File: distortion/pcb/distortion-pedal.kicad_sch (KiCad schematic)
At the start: 24 parts, among them U2 TL081H, U4 TL081H

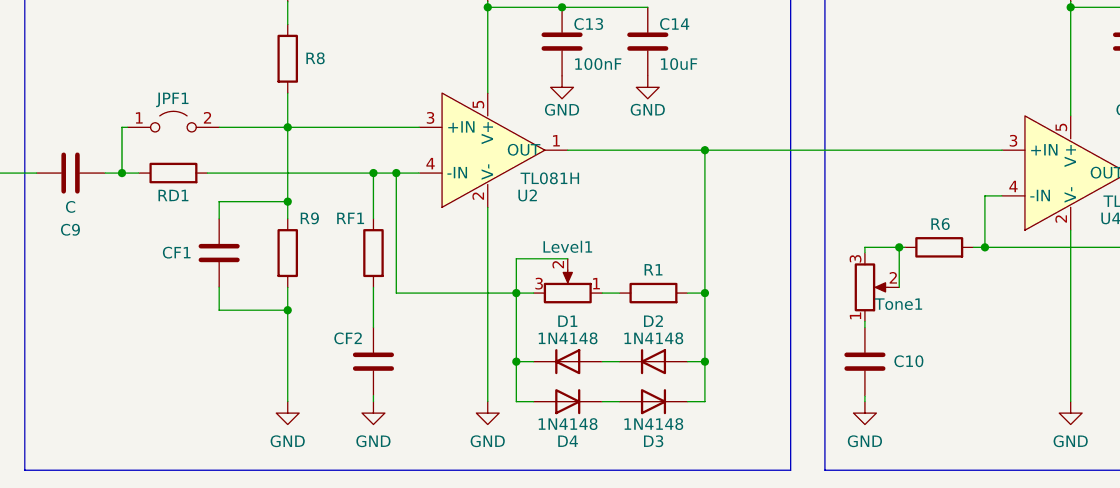
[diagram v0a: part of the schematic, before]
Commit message: add circuit dimensioning
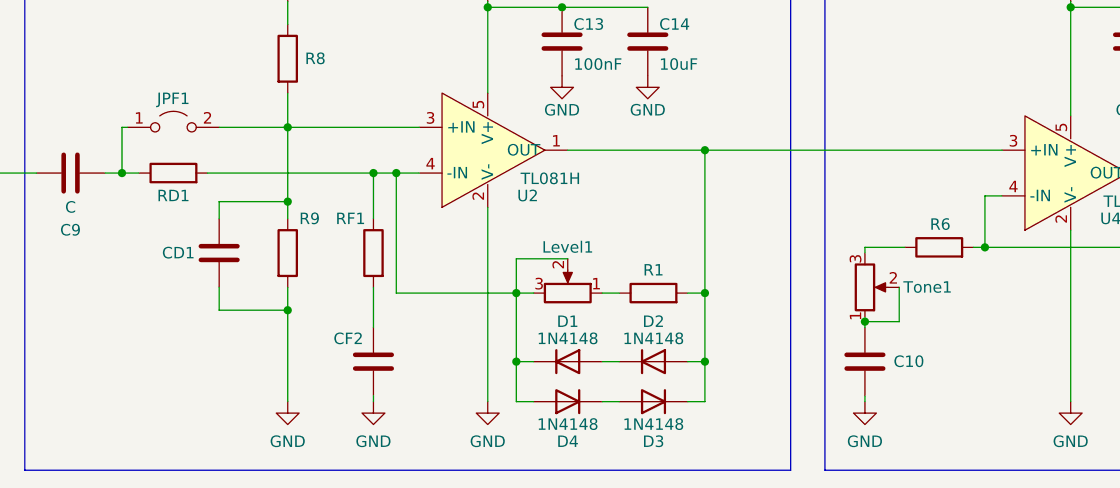
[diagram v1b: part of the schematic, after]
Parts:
- renumbered CF1 to CD1
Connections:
- net at C10.1, Tone1.1: now also Tone1.2
- net at R6.1, Tone1.3: no longer Tone1.2
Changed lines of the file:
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@@
   (junction (at 108.585 85.09) (diameter 0) (color 0 0 0 0)
   )
+  (junction (at 126.365 80.645) (diameter 0) (color 0 0 0 0)
+  )
   (junction (at 62.23 59.055) (diameter 0) (color 0 0 0 0)
   )
@@
   (junction (at 87.63 85.09) (diameter 0) (color 0 0 0 0)
   )
-  (junction (at 130.175 72.39) (diameter 0) (color 0 0 0 0)
-  )
   (wire (pts (xy 62.23 67.31) (xy 62.23 69.215))
     (stroke (width 0) (type default) (color 0 0 0 0))
@@
     (stroke (width 0) (type default) (color 0 0 0 0))
   )
-  (wire (pts (xy 130.81 72.39) (xy 130.175 72.39))
-    (stroke (width 0) (type default) (color 0 0 0 0))
-  )
   (wire (pts (xy 43.815 59.055) (xy 44.45 59.055))
     (stroke (width 0) (type default) (color 0 0 0 0))
@@
     (stroke (width 0) (type default) (color 0 0 0 0))
   )
+  (wire (pts (xy 130.175 80.645) (xy 126.365 80.645))
+    (stroke (width 0) (type default) (color 0 0 0 0))
+  )
   (wire (pts (xy 71.755 76.835) (xy 71.755 81.28))
     (stroke (width 0) (type default) (color 0 0 0 0))
@@
     (stroke (width 0) (type default) (color 0 0 0 0))
   )
-  (wire (pts (xy 130.175 72.39) (xy 130.175 76.835))
-    (stroke (width 0) (type default) (color 0 0 0 0))
-  )
   (wire (pts (xy 53.34 64.135) (xy 71.755 64.135))
     (stroke (width 0) (type default) (color 0 0 0 0))
@@
     (stroke (width 0) (type default) (color 0 0 0 0))
   )
+  (wire (pts (xy 130.175 76.835) (xy 130.175 80.645))
+    (stroke (width 0) (type default) (color 0 0 0 0))
+  )
   (wire (pts (xy 62.23 59.055) (xy 76.835 59.055))
     (stroke (width 0) (type default) (color 0 0 0 0))
@@
     (stroke (width 0) (type default) (color 0 0 0 0))
   )
-  (wire (pts (xy 130.175 72.39) (xy 126.365 72.39))
+  (wire (pts (xy 126.365 72.39) (xy 130.81 72.39))
     (stroke (width 0) (type default) (color 0 0 0 0))
   )
@@
   (symbol (lib_id "Device:R_Potentiometer") (at 126.365 76.835 0) (mirror x) (unit 1)
     (in_bom yes) (on_board yes)
-    (property "Reference" "Tone1" (id 0) (at 130.175 78.74 0))
+    (property "Reference" "Tone1" (id 0) (at 133.35 76.835 0))
     (property "Value" "R" (id 1) (at 131.445 76.835 90)
       (effects (font (size 1.27 1.27)) hide)
@@
   (symbol (lib_id "Device:C") (at 54.61 73.025 0) (unit 1)
     (in_bom yes) (on_board yes)
-    (property "Reference" "CF1" (id 0) (at 48.26 73.025 0)
+    (property "Reference" "CD1" (id 0) (at 48.26 73.025 0)
       (effects (font (size 1.27 1.27)) (justify left))
     )
@@
     )
     (path "/cff3208d-ece8-4d14-a5bb-ad4303e25136"
-      (reference "CF1") (unit 1) (value "C") (footprint "Capacitor_SMD:C_0805_2012Metric_Pad1.18x1.45mm_HandSolder")
+      (reference "CD1") (unit 1) (value "C") (footprint "Capacitor_SMD:C_0805_2012Metric_Pad1.18x1.45mm_HandSolder")
     )
     (path "/8086bab7-7dd2-4a38-97a8-11275acbbd45"

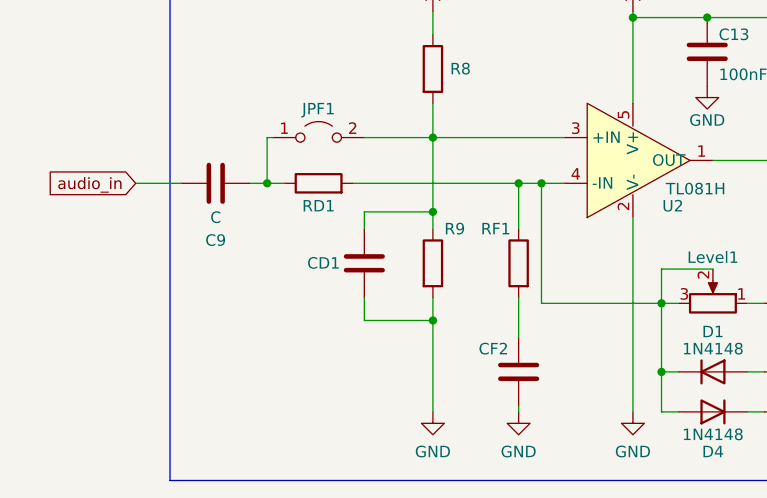
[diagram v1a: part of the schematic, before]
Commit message: add BOM, rework dimensioning
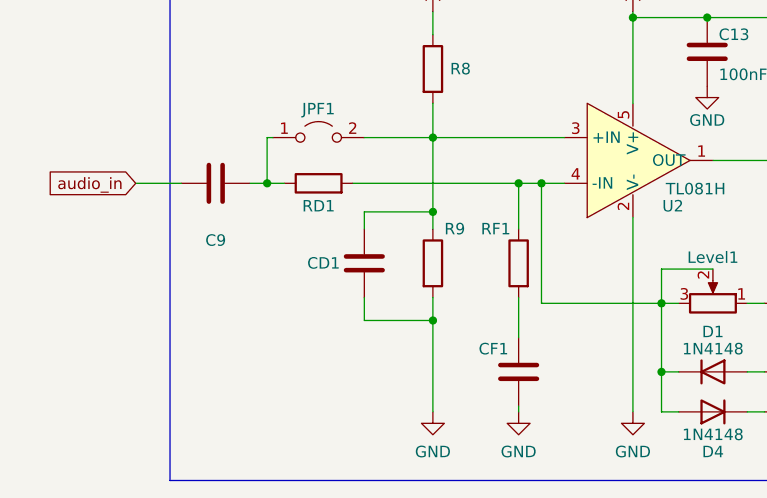
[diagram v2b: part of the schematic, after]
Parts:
- renumbered CF2 to CF1
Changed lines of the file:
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@@
     (in_bom yes) (on_board yes)
     (property "Reference" "C9" (id 0) (at 38.1 70.485 90))
-    (property "Value" "C" (id 1) (at 38.1 67.945 90))
+    (property "Value" "C" (id 1) (at 38.1 67.945 90)
+      (effects (font (size 1.27 1.27)) hide)
+    )
     (property "Footprint" "Capacitor_SMD:C_0805_2012Metric_Pad1.18x1.45mm_HandSolder" (id 2) (at 41.91 63.1698 0)
       (effects (font (size 1.27 1.27)) hide)
@@
   (symbol (lib_id "Device:C") (at 71.755 85.09 0) (unit 1)
     (in_bom yes) (on_board yes)
-    (property "Reference" "CF2" (id 0) (at 67.31 82.55 0)
+    (property "Reference" "CF1" (id 0) (at 67.31 82.55 0)
       (effects (font (size 1.27 1.27)) (justify left))
     )
@@
     )
     (path "/8086bab7-7dd2-4a38-97a8-11275acbbd45"
-      (reference "CF2") (unit 1) (value "C") (footprint "Capacitor_SMD:C_0805_2012Metric_Pad1.18x1.45mm_HandSolder")
+      (reference "CF1") (unit 1) (value "C") (footprint "Capacitor_SMD:C_0805_2012Metric_Pad1.18x1.45mm_HandSolder")
     )
     (path "/d2d7e7c8-e99d-4eb5-90cd-b5a50b0ad1d8"

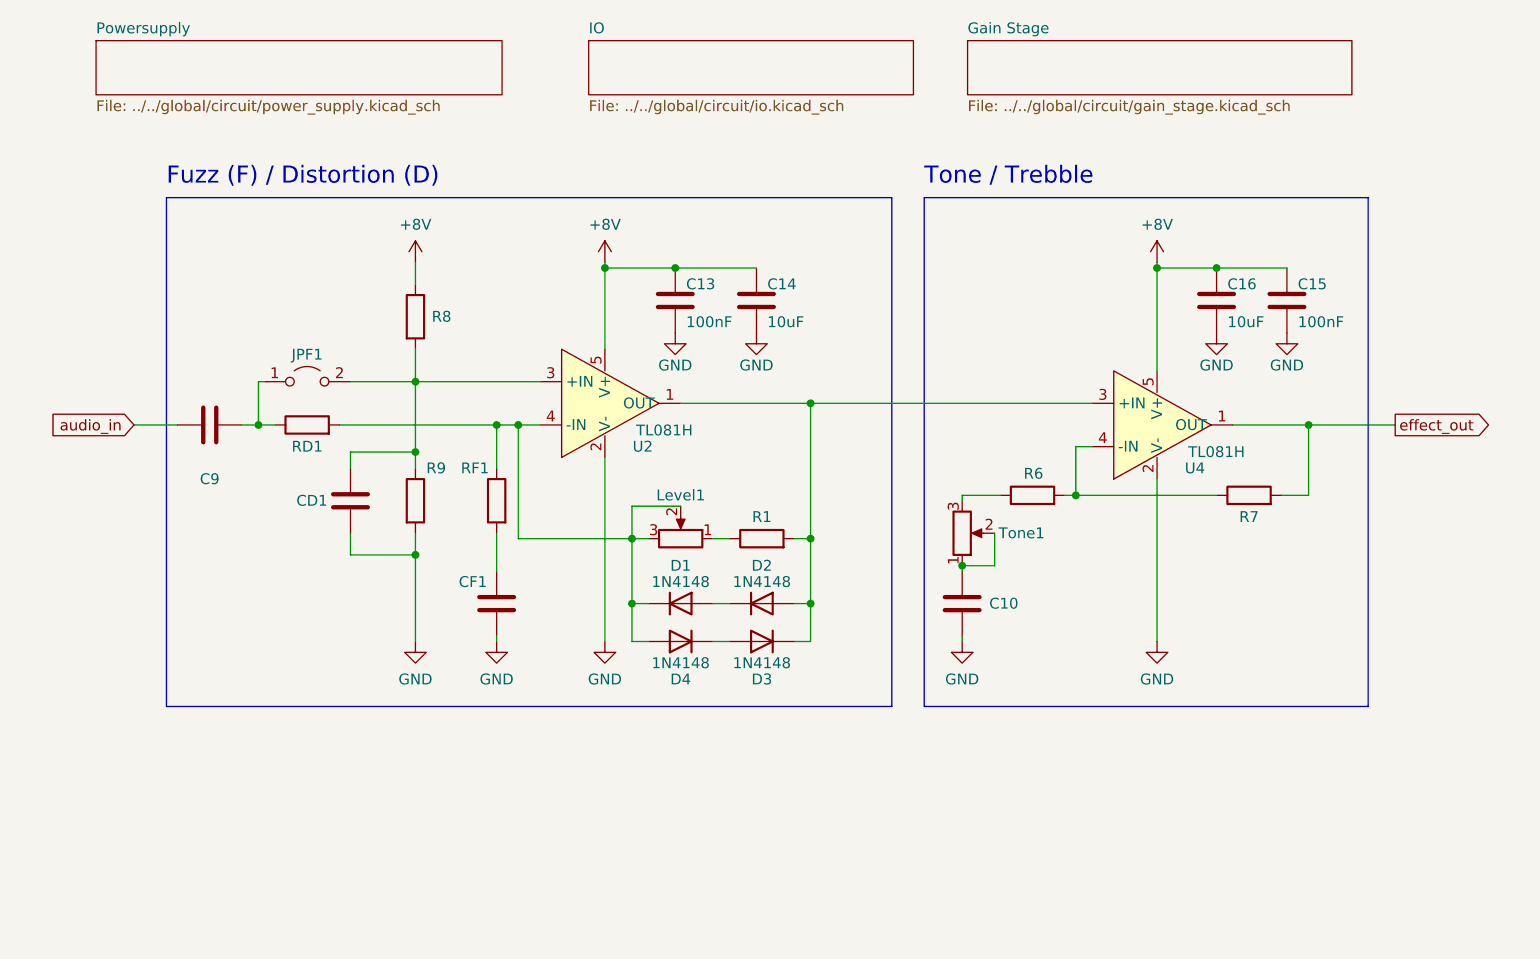
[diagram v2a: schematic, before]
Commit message: rework distortion circuit and simulations
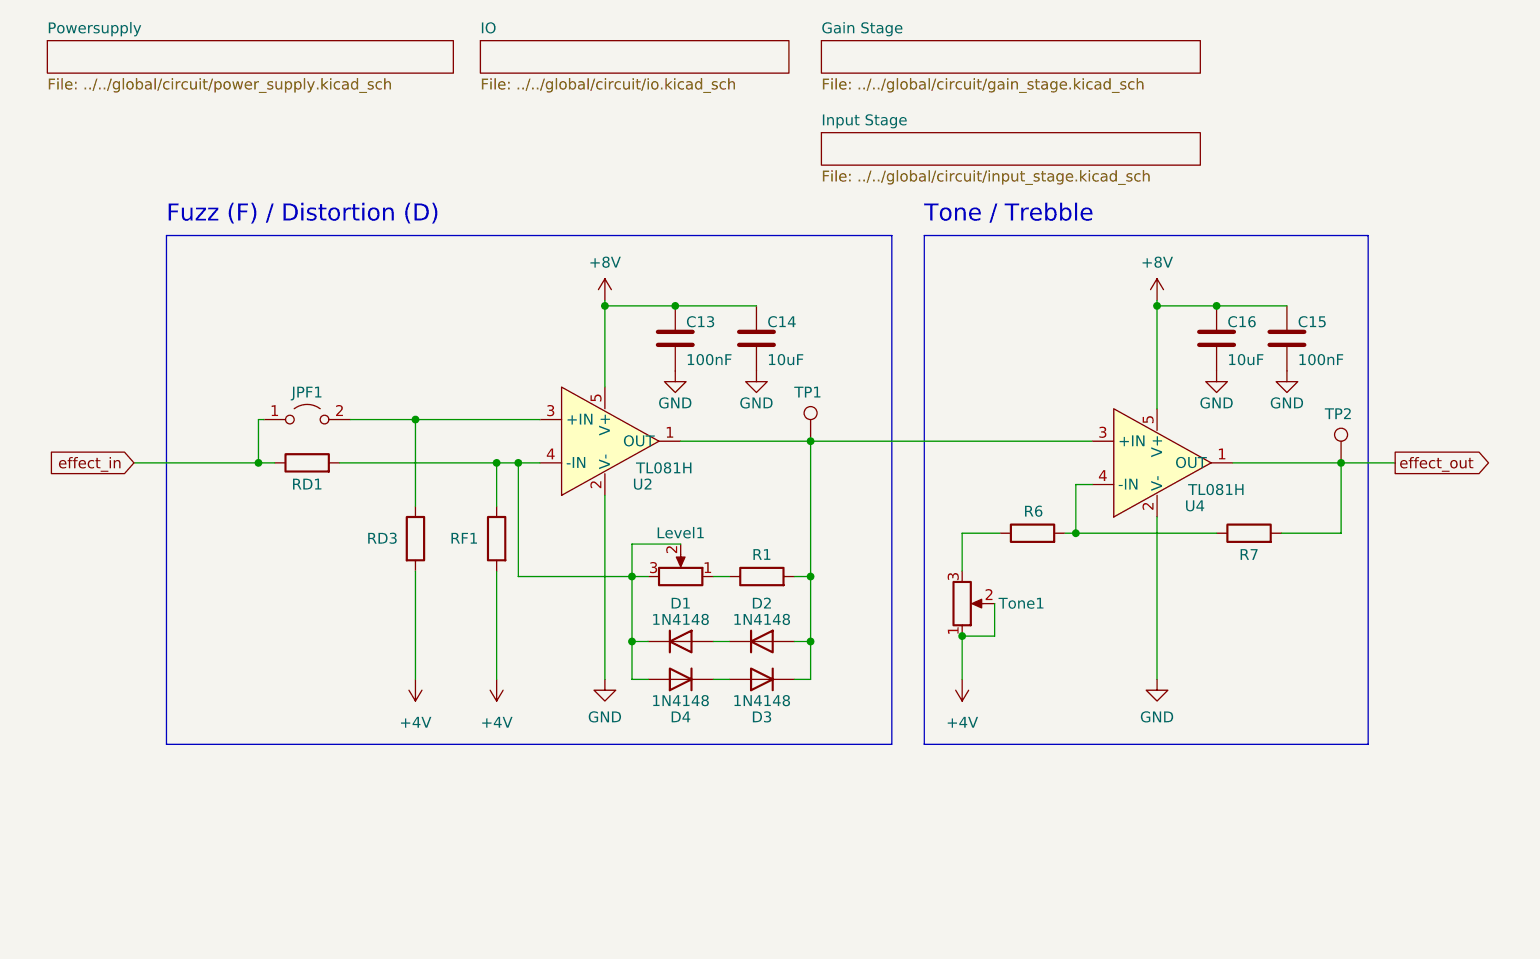
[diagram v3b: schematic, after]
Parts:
- removed C10, C9, CD1, CF1: C, Capacitor_SMD:C_0805_2012Metric_Pad1.18x1.45mm_HandSolder, symbol Device:C
- removed R8: R, Resistor_SMD:R_0805_2012Metric_Pad1.20x1.40mm_HandSolder, symbol Device:R
- added TP1, TP2: TestPoint, TestPoint:TestPoint_THTPad_1.0x1.0mm_Drill0.5mm, symbol Connector:TestPoint
- Level1, Tone1: footprint Potentiometer_THT:Potentiometer_Bourns_PTV09A-1_Single_Vertical -> Connector_PinHeader_2.54mm:PinHeader_1x03_P2.54mm_Vertical
- renumbered R9 to RD3
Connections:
- net GND: no longer RD3.2
- net effect_out: now also TP2.1
- net +4V: now reaches Tone1.1, Tone1.2
- net +4V: now also RD3.2, RF1.2
- net effect_in: now reaches JPF1.1 (A), RD1.1
- net at D2.2 (A), D3.1 (K), R1.2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: now also TP1.1
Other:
- added sheet Input Stage (../../global/circuit/input_stage.kicad_sch)
- moved on the sheet: C13, C14, C15, C16, D1, D2, D3, D4, JPF1, Level1, R1, R6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

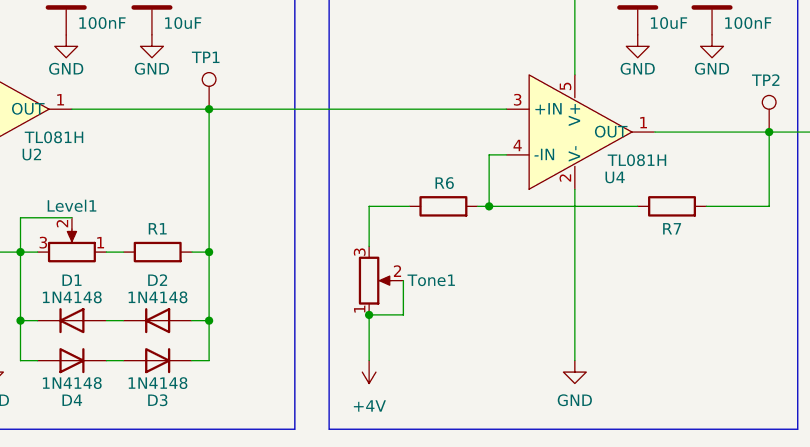
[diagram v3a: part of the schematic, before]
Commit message: create gerber files, update BOM for REV2
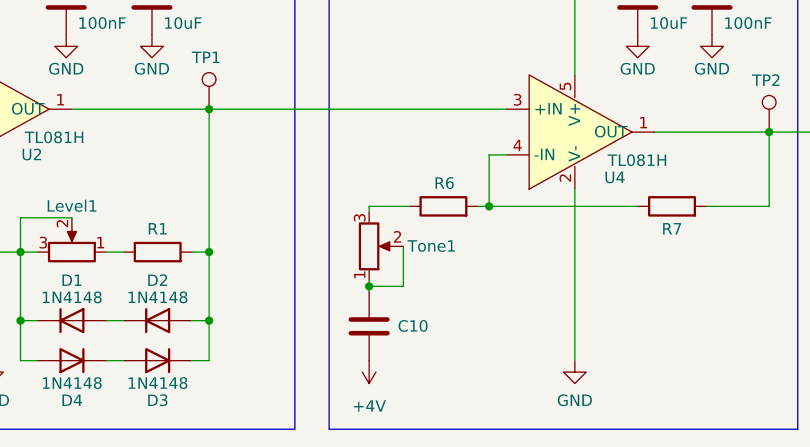
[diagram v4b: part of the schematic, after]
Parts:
- added C10: 10uF, Capacitor_SMD:C_0805_2012Metric_Pad1.18x1.45mm_HandSolder, symbol Device:C
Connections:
- net +4V: now also C10.2; no longer Tone1.1, Tone1.2
- new net: C10.1, Tone1.1, Tone1.2
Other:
- moved on the sheet: Tone1
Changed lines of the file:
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@@
   (title_block
     (title "Distortion Pedal")
-    (rev "1")
+    (rev "2")
   )
   (junction (at 108.585 89.535) (diameter 0) (color 0 0 0 0)
   )
-  (junction (at 126.365 88.9) (diameter 0) (color 0 0 0 0)
-  )
   (junction (at 62.23 63.5) (diameter 0) (color 0 0 0 0)
   )
@@
   (junction (at 87.63 89.535) (diameter 0) (color 0 0 0 0)
   )
+  (junction (at 126.365 85.725) (diameter 0) (color 0 0 0 0)
+  )
   (wire (pts (xy 29.21 68.58) (xy 43.815 68.58))
     (stroke (width 0) (type default) (color 0 0 0 0))
@@
     (stroke (width 0) (type default) (color 0 0 0 0))
   )
-  (wire (pts (xy 130.175 88.9) (xy 126.365 88.9))
+  (wire (pts (xy 130.175 85.725) (xy 126.365 85.725))
     (stroke (width 0) (type default) (color 0 0 0 0))
   )
@@
     (stroke (width 0) (type default) (color 0 0 0 0))
   )
+  (wire (pts (xy 126.365 85.09) (xy 126.365 85.725))
+    (stroke (width 0) (type default) (color 0 0 0 0))
+  )
   (wire (pts (xy 170.815 68.58) (xy 177.165 68.58))
     (stroke (width 0) (type default) (color 0 0 0 0))
@@
     (stroke (width 0) (type default) (color 0 0 0 0))
   )
-  (wire (pts (xy 126.365 81.28) (xy 126.365 76.835))
+  (wire (pts (xy 126.365 77.47) (xy 126.365 76.835))
     (stroke (width 0) (type default) (color 0 0 0 0))
   )
@@
     (stroke (width 0) (type default) (color 0 0 0 0))
   )
-  (wire (pts (xy 130.175 85.09) (xy 130.175 88.9))
+  (wire (pts (xy 126.365 85.725) (xy 126.365 86.36))
+    (stroke (width 0) (type default) (color 0 0 0 0))
+  )
+  (wire (pts (xy 130.175 81.28) (xy 130.175 85.725))
     (stroke (width 0) (type default) (color 0 0 0 0))
   )
@@
   )
   (wire (pts (xy 71.755 68.58) (xy 71.755 73.66))
-    (stroke (width 0) (type default) (color 0 0 0 0))
-  )
-  (wire (pts (xy 126.365 88.9) (xy 126.365 93.98))
     (stroke (width 0) (type default) (color 0 0 0 0))
   )
@@
     (pin "2")
   )
-  (symbol (lib_id "Device:R_Potentiometer") (at 126.365 85.09 0) (mirror x) (unit 1)
-    (in_bom yes) (on_board yes)
-    (property "Reference" "Tone1" (id 0) (at 133.35 85.09 0))
-    (property "Value" "R" (id 1) (at 131.445 85.09 90)
-      (effects (font (size 1.27 1.27)) hide)
-    )
-    (property "Footprint" "Connector_PinHeader_2.54mm:PinHeader_1x03_P2.54mm_Vertical" (id 2) (at 126.365 85.09 0)
-      (effects (font (size 1.27 1.27)) hide)
-    )
-    (property "Datasheet" "~" (id 3) (at 126.365 85.09 0)
+  (symbol (lib_id "Device:R_Potentiometer") (at 126.365 81.28 0) (mirror x) (unit 1)
+    (in_bom yes) (on_board yes)
+    (property "Reference" "Tone1" (id 0) (at 133.35 81.28 0))
+    (property "Value" "R" (id 1) (at 131.445 81.28 90)
+      (effects (font (size 1.27 1.27)) hide)
+    )
+    (property "Footprint" "Connector_PinHeader_2.54mm:PinHeader_1x03_P2.54mm_Vertical" (id 2) (at 126.365 81.28 0)
+      (effects (font (size 1.27 1.27)) hide)
+    )
+    (property "Datasheet" "~" (id 3) (at 126.365 81.28 0)
       (effects (font (size 1.27 1.27)) hide)
     )
@@
     )
     (property "Datasheet" "~" (id 3) (at 102.87 81.915 0)
+      (effects (font (size 1.27 1.27)) hide)
+    )
+    (pin "1")
+    (pin "2")
+  )
+  (symbol (lib_id "Device:C") (at 126.365 90.17 0) (unit 1)
+    (in_bom yes) (on_board yes)
+    (property "Reference" "C10" (id 0) (at 129.54 90.17 0)
+      (effects (font (size 1.27 1.27)) (justify left))
+    )
+    (property "Value" "10uF" (id 1) (at 127.635 92.71 0)
+      (effects (font (size 1.27 1.27)) (justify left) hide)
+    )
+    (property "Footprint" "Capacitor_SMD:C_0805_2012Metric_Pad1.18x1.45mm_HandSolder" (id 2) (at 127.3302 93.98 0)
+      (effects (font (size 1.27 1.27)) hide)
+    )
+    (property "Datasheet" "~" (id 3) (at 126.365 90.17 0)
       (effects (font (size 1.27 1.27)) hide)
     )
@@
       (reference "C8") (unit 1) (value "C") (footprint "Capacitor_SMD:C_0805_2012Metric_Pad1.18x1.45mm_HandSolder")
     )
+    (path "/a2f80fad-1419-4aa8-a5a7-ebe7dbd1ad61"
+      (reference "C10") (unit 1) (value "10uF") (footprint "Capacitor_SMD:C_0805_2012Metric_Pad1.18x1.45mm_HandSolder")
+    )
     (path "/e58f7600-ef75-4a2a-9068-bd03a6cb5330/c122b5fc-4200-46e9-bbe3-fa90ca959909"

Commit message: distortion rev 3
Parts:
- added R9, RF2: R, Resistor_SMD:R_0805_2012Metric_Pad1.20x1.40mm_HandSolder, symbol Device:R
- Level1: footprint Connector_PinHeader_2.54mm:PinHeader_1x03_P2.54mm_Vertical -> effect_pedal:potentiometer_wired_23_connected
- Tone1: footprint Connector_PinHeader_2.54mm:PinHeader_1x03_P2.54mm_Vertical -> effect_pedal:potentiometer_wired_12_connected
- renumbered RD3 to R18
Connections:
- net +4V: now also RF2.1
- net effect_in: now also R9.2; no longer JPF1.1 (A), RD1.1
- new net: JPF1.1 (A), R9.1, RD1.1, RF2.2
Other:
- note added: "Distortion"
- note added: "Fuzz"
- note added: "close: JPF1 use: RF1, RF2 Don't use: RD1"
- note added: "open: JPF1 use: RD1 Don't use: RF1, RF2"
- moved on the sheet: C10, C13, C14, C15, C16, D1, D2, D3, D4, JPF1, Level1, R1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
